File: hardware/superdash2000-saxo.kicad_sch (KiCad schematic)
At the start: 13 parts, among them J1 Molex 34691-0161, U1 L7805, U1 TLV2372

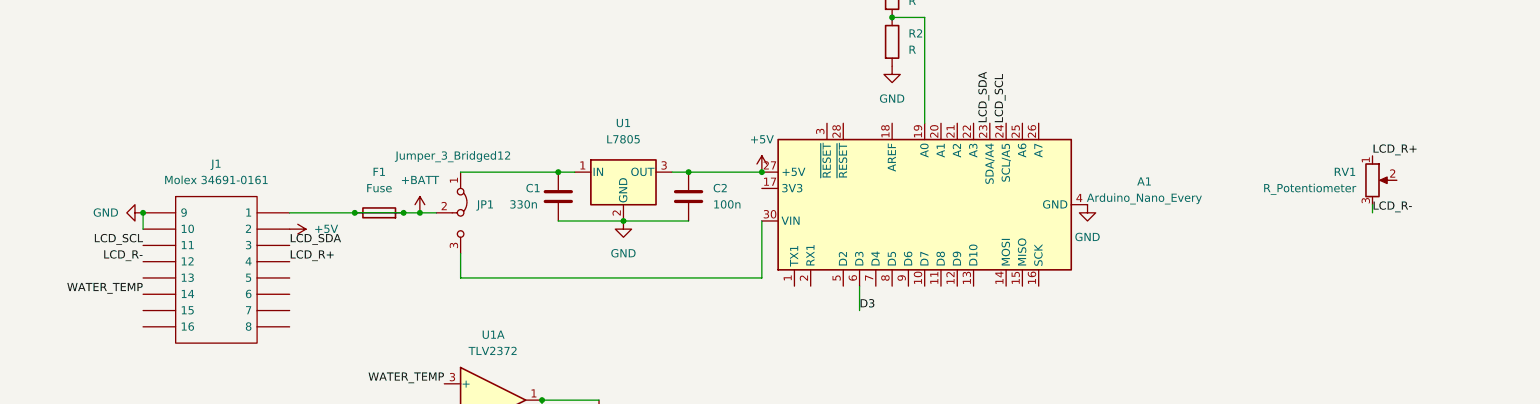
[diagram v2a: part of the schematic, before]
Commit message: hardware: s/LCD_R/LCD_BRIGHTNESS + fix pin used on pot
Signed-off-by: Thomas Antonini <antonini.thomas@gmail.com>
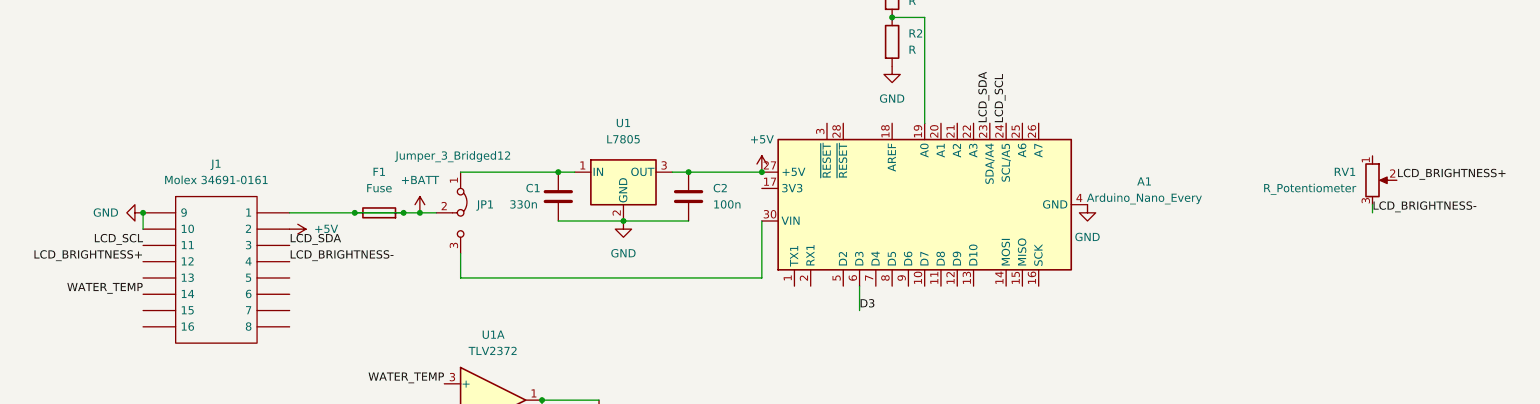
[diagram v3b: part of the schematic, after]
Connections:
- net LCD_BRIGHTNESS+: now reaches RV1.2
- net LCD_BRIGHTNESS+: now also J1.12
- net LCD_R+: no longer names the net of RV1.1
- net LCD_R+: no longer J1.4
- net LCD_R- renamed LCD_BRIGHTNESS-
- net LCD_BRIGHTNESS-: now also J1.4; no longer J1.12
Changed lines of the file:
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@@
-    (effects (font (size 1.27 1.27)) (justify left bottom))
-  )
-  (label "LCD_R+" (at 60.96 72.39 0)
     (effects (font (size 1.27 1.27)) (justify left bottom))
   )
@@
     (effects (font (size 1.27 1.27)) (justify right bottom))
   )
-  (label "LCD_R+" (at 229.87 55.88 0)
+  (label "LCD_SDA" (at 60.96 69.85 0)
     (effects (font (size 1.27 1.27)) (justify left bottom))
   )
-  (label "LCD_SDA" (at 60.96 69.85 0)
+  (label "LCD_BRIGHTNESS-" (at 229.87 64.77 0)
     (effects (font (size 1.27 1.27)) (justify left bottom))
+  )
+  (label "LCD_BRIGHTNESS+" (at 38.1 72.39 180)
+    (effects (font (size 1.27 1.27)) (justify right bottom))
   )
   (label "WATER_TEMP" (at 85.09 91.44 180)
     (effects (font (size 1.27 1.27)) (justify right bottom))
   )
+  (label "LCD_BRIGHTNESS-" (at 60.96 72.39 0)
+    (effects (font (size 1.27 1.27)) (justify left bottom))
+  )
   (label "LCD_SCL" (at 38.1 69.85 180)
     (effects (font (size 1.27 1.27)) (justify right bottom))
   )
-  (label "LCD_R-" (at 38.1 72.39 180)
-    (effects (font (size 1.27 1.27)) (justify right bottom))
+  (label "LCD_BRIGHTNESS+" (at 233.68 59.69 0)
+    (effects (font (size 1.27 1.27)) (justify left bottom))
   )
   (label "D3" (at 109.22 102.87 0)
@@
     (effects (font (size 1.27 1.27)) (justify left bottom))
   )
-  (label "LCD_R-" (at 229.87 64.77 0)
-    (effects (font (size 1.27 1.27)) (justify left bottom))
-  )

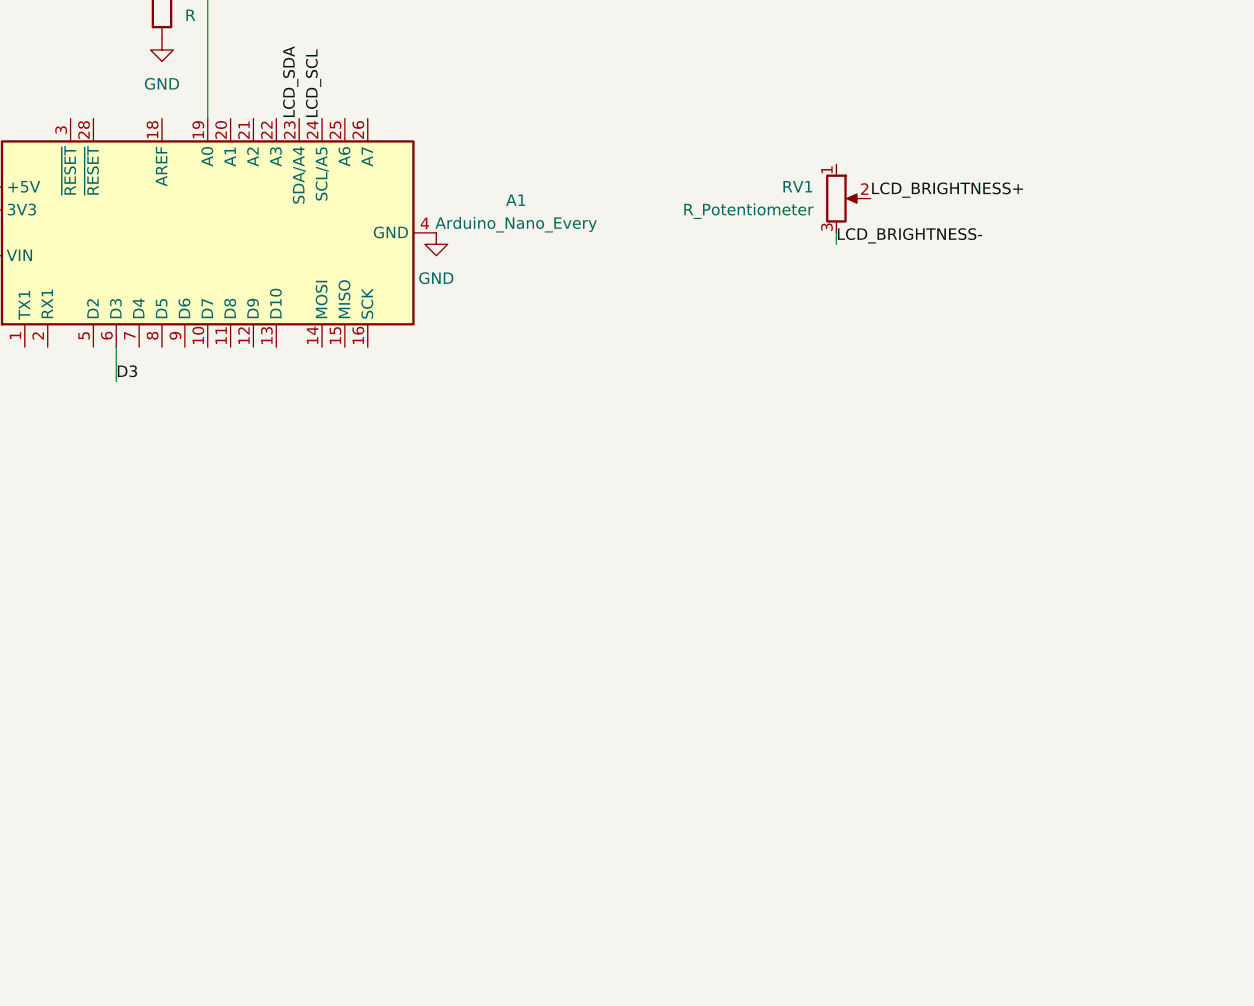
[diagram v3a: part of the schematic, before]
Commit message: hardware: Replace lcd brightness pot by mux
Signed-off-by: Thomas Antonini <antonini.thomas@gmail.com>
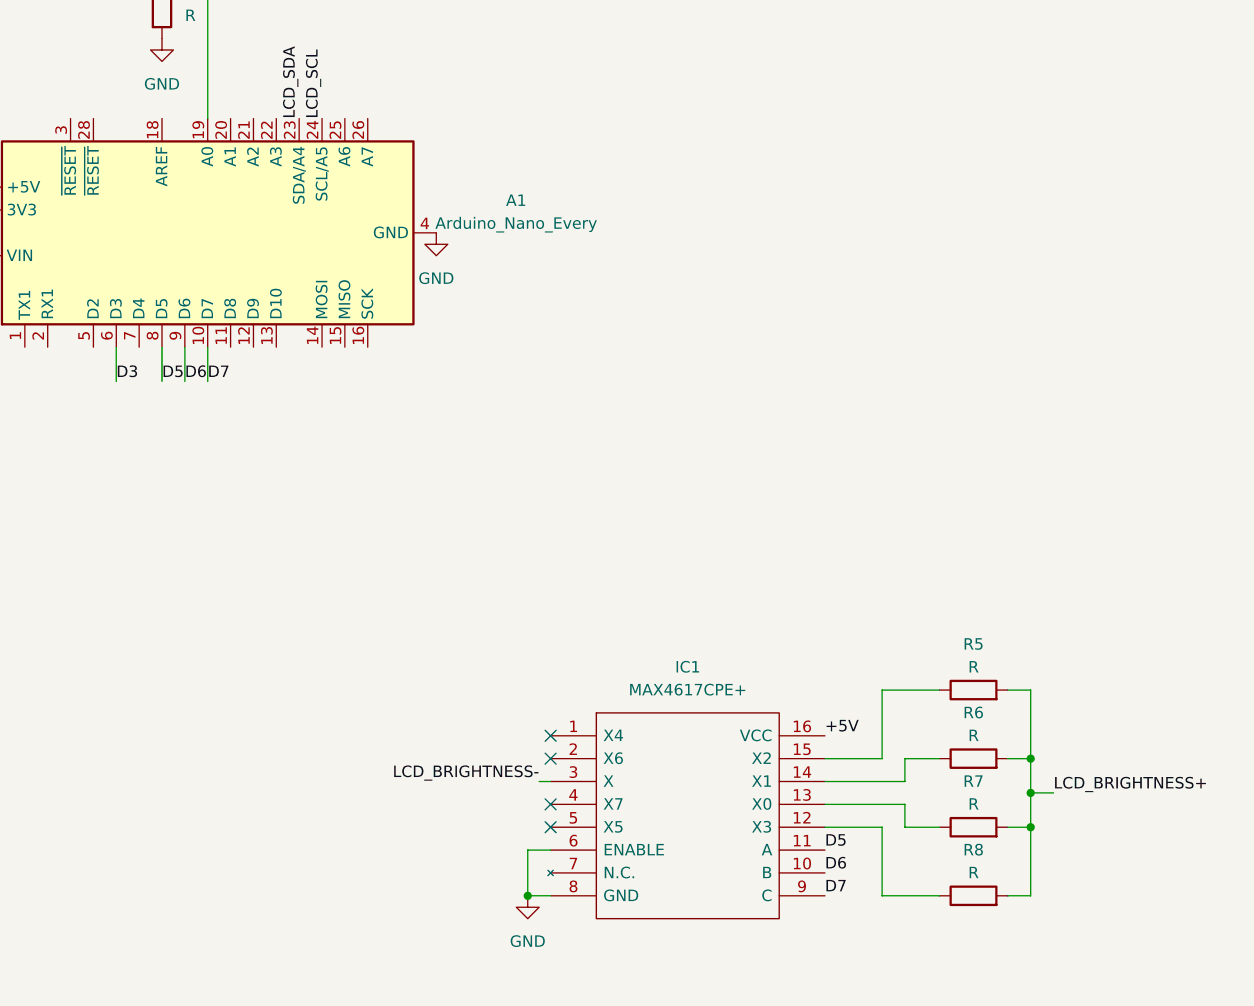
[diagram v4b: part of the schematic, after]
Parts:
- removed RV1: R_Potentiometer, symbol Device:R_Potentiometer
- added IC1: MAX4617CPE+, DIP794W56P254L1918H457Q16N, symbol MAX4617CPE+:MAX4617CPE+
- added R5, R6, R7, R8: R, symbol Device:R
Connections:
- net +5V: now also IC1.16 (VCC)
- net GND: now also IC1.6 (ENABLE), IC1.8 (GND)
- net LCD_BRIGHTNESS+: now also R5.2, R6.2, R7.2, R8.2
- net LCD_BRIGHTNESS-: now also IC1.3 (X)
- net D7: now reaches A1.10 (D7)
- net D7: now also IC1.9 (C)
- net D5: now reaches A1.8 (D5)
- net D5: now also IC1.11 (A)
- net D6: now reaches A1.9 (D6)
- net D6: now also IC1.10 (B)
- new net: IC1.15 (X2), R5.1
- new net: IC1.14 (X1), R6.1
- new net: IC1.12 (X3), R8.1
- new net: IC1.13 (X0), R7.1
- no-connect marks 3 -> 7

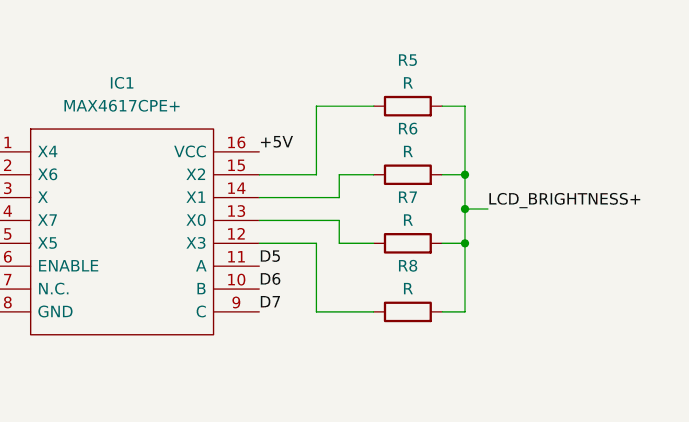
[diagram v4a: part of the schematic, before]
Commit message: hardware: Replace 2 R LCD brigthness by pots
Signed-off-by: Thomas Antonini <antonini.thomas@gmail.com>
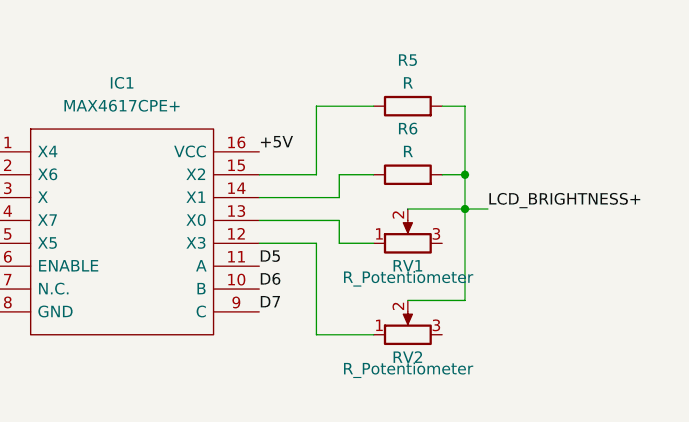
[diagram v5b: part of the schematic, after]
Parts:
- removed R7, R8: R, symbol Device:R
- added RV1, RV2: R_Potentiometer, symbol Device:R_Potentiometer
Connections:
- net LCD_BRIGHTNESS+: now also RV1.2, RV2.2
- net at IC1.12 (X3): now also RV2.1
- net at IC1.13 (X0): now also RV1.1

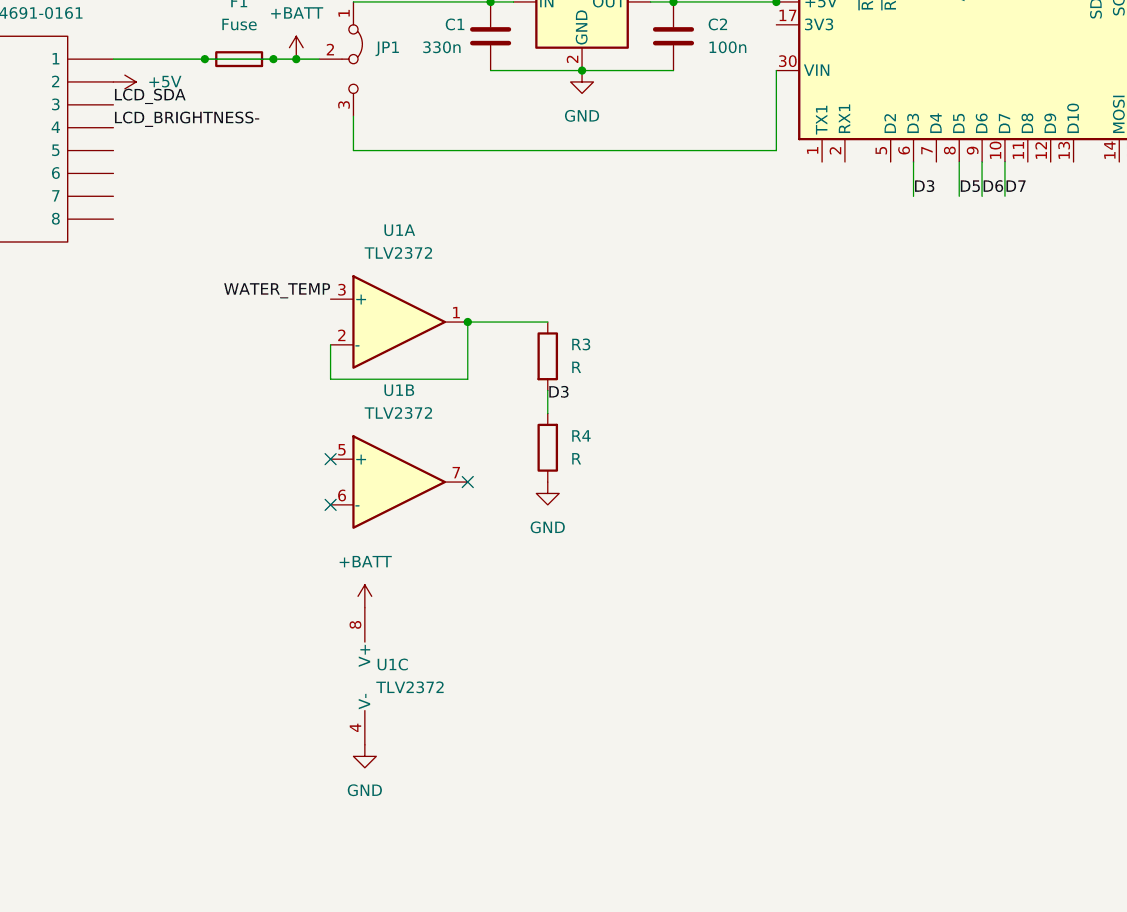
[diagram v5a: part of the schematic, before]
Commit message: hardware: Add dimmer
Signed-off-by: Thomas Antonini <antonini.thomas@gmail.com>
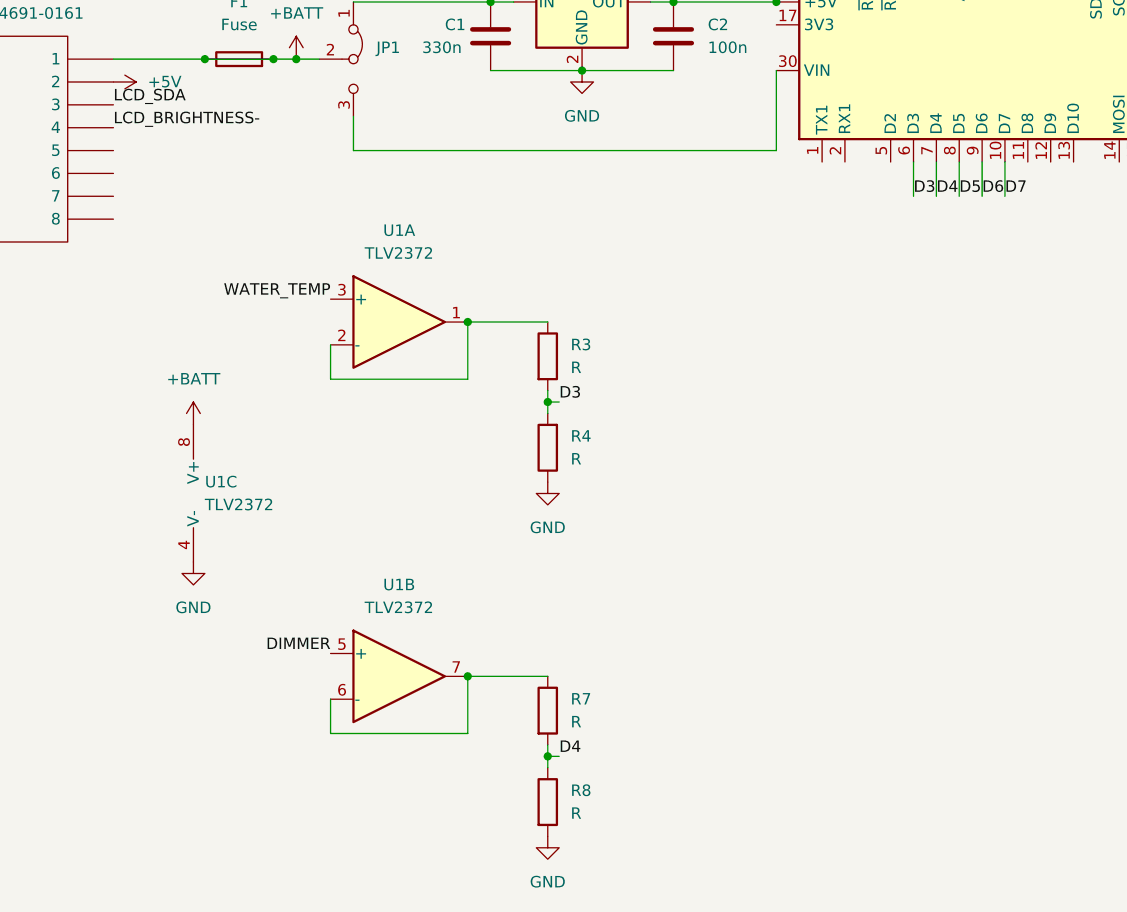
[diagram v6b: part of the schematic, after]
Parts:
- added R7, R8: R, symbol Device:R
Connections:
- net GND: now also R8.2
- net D4: now reaches A1.7 (D4)
- net D4: now also R7.2, R8.1
- net DIMMER: now reaches U1.5 (+)
- net at U1.6 (-): now also U1.7, R7.1
- no-connect marks 7 -> 4
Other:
- moved on the sheet: U1B, U1C
